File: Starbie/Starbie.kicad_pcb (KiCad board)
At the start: 2 copper layers, 130.6 x 90.5 mm, 8 parts, among them J1 Conn_01x04_Pin, J2 Conn_01x08_Pin, SW1 SW_Push, SW2 SW_Push, U1 XIAO-ESP32-C3-SMD, U2 DHT11

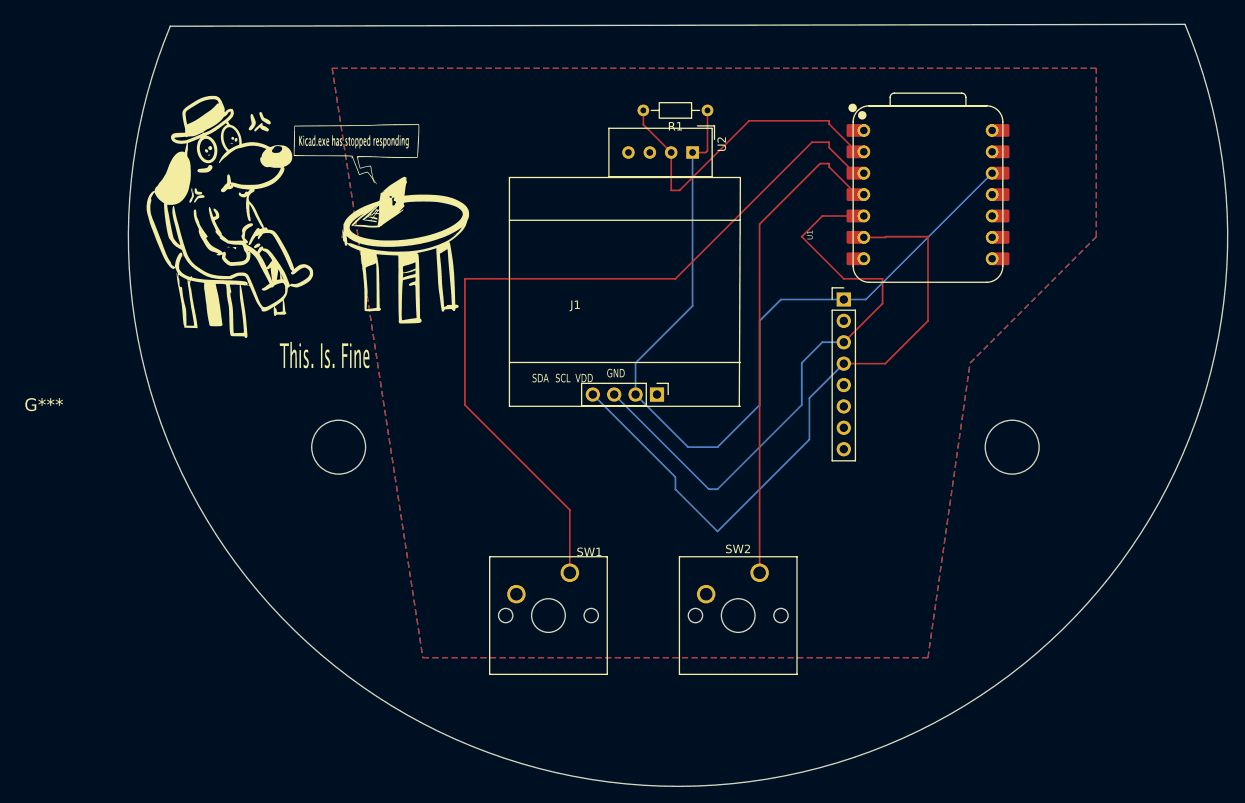
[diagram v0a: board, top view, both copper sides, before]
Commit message: feat- added piezo buzzer to PCB
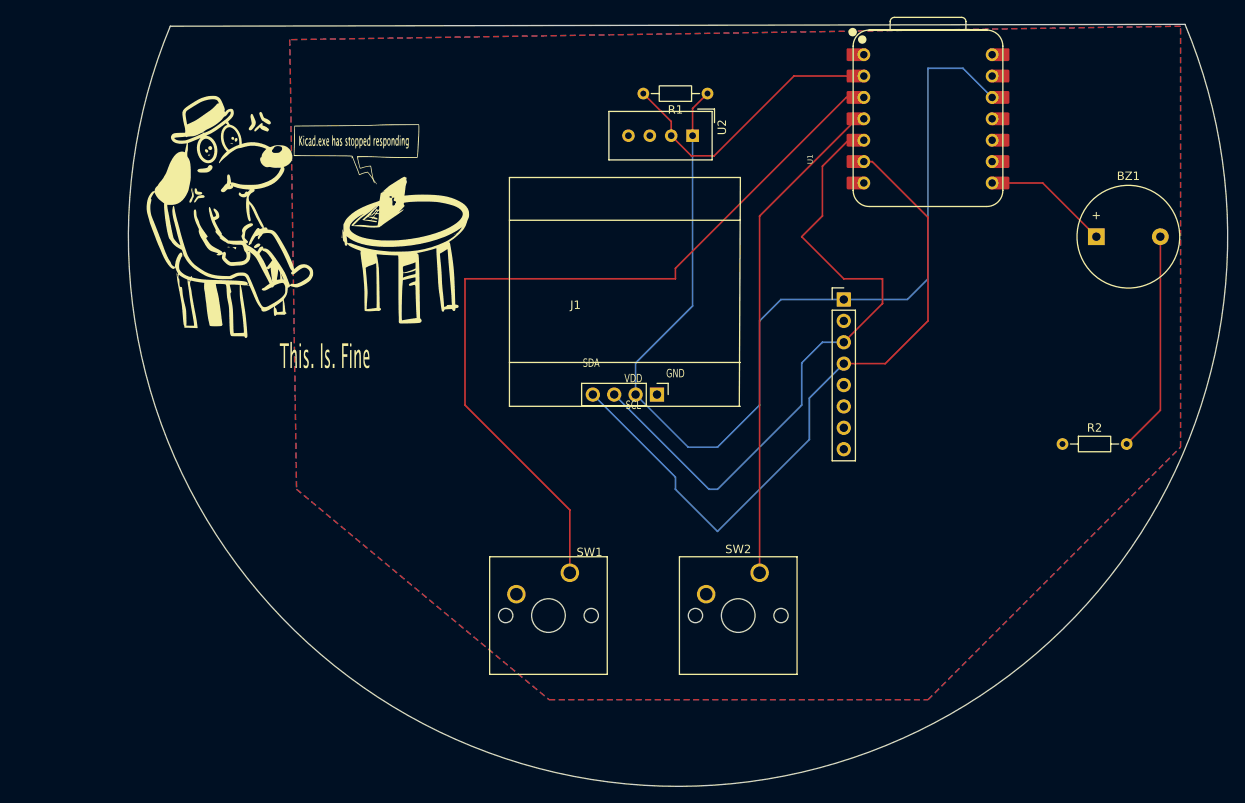
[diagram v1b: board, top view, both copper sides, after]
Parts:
- added BZ1: Buzzer, Buzzer_Beeper:Buzzer_12x9.5RM7.6, F.Cu at (175.0, 75.0)
- added R2: 100, Resistor_THT:R_Axial_DIN0204_L3.6mm_D1.6mm_P7.62mm_Horizontal, F.Cu at (171.0, 99.6)
- moved U1 9.00 mm to (155.0, 61.0)
- moved R1 2.00 mm to (128.8, 58.0)
- moved U2 2.00 mm to (127.0, 63.0)
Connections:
- net /DIO 2 renamed /GPIO 2
- net /DIO 3 renamed /GPIO 3
- U1 pad 8: unconnected-(U1-D7-Pad8) -> /GPIO 20
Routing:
- net Net-(BZ1--): track 0.00 -> 26.3 mm
- net +3.3V: track 102.5 -> 124.8 mm
- net /GPIO 20: track 0.00 -> 14.2 mm
- net /SCL: track 71.6 -> 78.8 mm
- net /SDA: track 78.3 -> 83.3 mm
- net /DHT11 DATA: track 38.1 -> 34.2 mm
- net /GPIO 3: track 57.7 -> 59.5 mm
- net /GPIO 2: track 96.1 -> 97.1 mm
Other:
- outline, holes or cut-outs redrawn
